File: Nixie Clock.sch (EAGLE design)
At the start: 153 parts, among them IC1_SECONDS_UNITS 4017N, IC2_SECONDS_TENS 4017N, IC3_MINUTES_UNITS 4017N, IC4_MINUTES_TENS 4017N, IC5_HOURS_UNITS 4017N, IC6_HOURS_TENS 4017N, IC7_AND 4081N, T0 MPSA42, T1 MPSA42, T10 MPSA42, T11 MPSA42, T12 MPSA42, T13 MPSA42, T14 MPSA42, T15 MPSA42, T16 MPSA42, T17 MPSA42, T18 MPSA42, T19 MPSA42, T2 MPSA42, T20 MPSA42, T21 MPSA42, T22 MPSA42, T23 MPSA42, T24 MPSA42, T25 MPSA42, T26 MPSA42, T27 MPSA42, T28 MPSA42, T29 MPSA42, T3 MPSA42, T30 MPSA42, T31 MPSA42, T32 MPSA42, T33 MPSA42, T34 MPSA42, T35 MPSA42, T36 MPSA42, T37 MPSA42, T38 MPSA42, T39 MPSA42, T4 MPSA42, T40 MPSA42, T41 MPSA42, T42 MPSA42, T43 MPSA42, T44 MPSA42, T5 MPSA42, T6 MPSA42, T7 MPSA42, T8 MPSA42, T9 MPSA42

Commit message: Use an alternative package for tubes, with bigger pads
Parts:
- HOURS_TENS, HOURS_UNITS, MINUTES_TENS, MINUTES_UNITS, SECONDS_TENS, SECONDS_UNITS: value IN-14 -> IN-14BIG_PADS; device PGT:IN-14 -> PGT:IN-14BIG_PADS
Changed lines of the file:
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@@
 <grid distance="0.1" unitdist="inch" unit="inch" style="lines" multiple="1" display="no" altdistance="0.01" altunitdist="inch" altunit="inch"/>
 <layers>
-<layer number="1" name="Top" color="4" fill="1" visible="no" active="no"/>
-<layer number="2" name="Route2" color="1" fill="3" visible="no" active="no"/>
-<layer number="3" name="Route3" color="4" fill="3" visible="no" active="no"/>
-<layer number="4" name="Route4" color="1" fill="4" visible="no" active="no"/>
-<layer number="5" name="Route5" color="4" fill="4" visible="no" active="no"/>
-<layer number="6" name="Route6" color="1" fill="8" visible="no" active="no"/>
-<layer number="7" name="Route7" color="4" fill="8" visible="no" active="no"/>
-<layer number="8" name="Route8" color="1" fill="2" visible="no" active="no"/>
-<layer number="9" name="Route9" color="4" fill="2" visible="no" active="no"/>
-<layer number="10" name="Route10" color="1" fill="7" visible="no" active="no"/>
-<layer number="11" name="Route11" color="4" fill="7" visible="no" active="no"/>
-<layer number="12" name="Route12" color="1" fill="5" visible="no" active="no"/>
-<layer number="13" name="Route13" color="4" fill="5" visible="no" active="no"/>
-<layer number="14" name="Route14" color="1" fill="6" visible="no" active="no"/>
-<layer number="15" name="Route15" color="4" fill="6" visible="no" active="no"/>
-<layer number="16" name="Bottom" color="1" fill="1" visible="no" active="no"/>
-<layer number="17" name="Pads" color="2" fill="1" visible="no" active="no"/>
-<layer number="18" name="Vias" color="2" fill="1" visible="no" active="no"/>
-<layer number="19" name="Unrouted" color="6" fill="1" visible="no" active="no"/>
-<layer number="20" name="Dimension" color="15" fill="1" visible="no" active="no"/>
-<layer number="21" name="tPlace" color="7" fill="1" visible="no" active="no"/>
-<layer number="22" name="bPlace" color="7" fill="1" visible="no" active="no"/>
-<layer number="23" name="tOrigins" color="15" fill="1" visible="no" active="no"/>
-<layer number="24" name="bOrigins" color="15" fill="1" visible="no" active="no"/>
-<layer number="25" name="tNames" color="7" fill="1" visible="no" active="no"/>
-<layer number="26" name="bNames" color="7" fill="1" visible="no" active="no"/>
-<layer number="27" name="tValues" color="7" fill="1" visible="no" active="no"/>
-<layer number="28" name="bValues" color="7" fill="1" visible="no" active="no"/>
+<layer number="1" name="Top" color="4" fill="1" visible="yes" active="no"/>
+<layer number="2" name="Route2" color="1" fill="3" visible="yes" active="no"/>
+<layer number="3" name="Route3" color="4" fill="3" visible="yes" active="no"/>
+<layer number="4" name="Route4" color="1" fill="4" visible="yes" active="no"/>
+<layer number="5" name="Route5" color="4" fill="4" visible="yes" active="no"/>
+<layer number="6" name="Route6" color="1" fill="8" visible="yes" active="no"/>
+<layer number="7" name="Route7" color="4" fill="8" visible="yes" active="no"/>
+<layer number="8" name="Route8" color="1" fill="2" visible="yes" active="no"/>
+<layer number="9" name="Route9" color="4" fill="2" visible="yes" active="no"/>
+<layer number="10" name="Route10" color="1" fill="7" visible="yes" active="no"/>
+<layer number="11" name="Route11" color="4" fill="7" visible="yes" active="no"/>
+<layer number="12" name="Route12" color="1" fill="5" visible="yes" active="no"/>
+<layer number="13" name="Route13" color="4" fill="5" visible="yes" active="no"/>
+<layer number="14" name="Route14" color="1" fill="6" visible="yes" active="no"/>
+<layer number="15" name="Route15" color="4" fill="6" visible="yes" active="no"/>
+<layer number="16" name="Bottom" color="1" fill="1" visible="yes" active="no"/>
+<layer number="17" name="Pads" color="2" fill="1" visible="yes" active="no"/>
+<layer number="18" name="Vias" color="2" fill="1" visible="yes" active="no"/>
+<layer number="19" name="Unrouted" color="6" fill="1" visible="yes" active="no"/>
+<layer number="20" name="Dimension" color="15" fill="1" visible="yes" active="no"/>
+<layer number="21" name="tPlace" color="7" fill="1" visible="yes" active="no"/>
+<layer number="22" name="bPlace" color="7" fill="1" visible="yes" active="no"/>
+<layer number="23" name="tOrigins" color="15" fill="1" visible="yes" active="no"/>
+<layer number="24" name="bOrigins" color="15" fill="1" visible="yes" active="no"/>
+<layer number="25" name="tNames" color="7" fill="1" visible="yes" active="no"/>
+<layer number="26" name="bNames" color="7" fill="1" visible="yes" active="no"/>
+<layer number="27" name="tValues" color="7" fill="1" visible="yes" active="no"/>
+<layer number="28" name="bValues" color="7" fill="1" visible="yes" active="no"/>
 <layer number="29" name="tStop" color="7" fill="3" visible="no" active="no"/>
 <layer number="30" name="bStop" color="7" fill="6" visible="no" active="no"/>
@@
 <layer number="35" name="tGlue" color="7" fill="4" visible="no" active="no"/>
 <layer number="36" name="bGlue" color="7" fill="5" visible="no" active="no"/>
-<layer number="37" name="tTest" color="7" fill="1" visible="no" active="no"/>
-<layer number="38" name="bTest" color="7" fill="1" visible="no" active="no"/>
+<layer number="37" name="tTest" color="7" fill="1" visible="yes" active="no"/>
+<layer number="38" name="bTest" color="7" fill="1" visible="yes" active="no"/>
 <layer number="39" name="tKeepout" color="4" fill="11" visible="no" active="no"/>
 <layer number="40" name="bKeepout" color="1" fill="11" visible="no" active="no"/>
@@
 <layer number="44" name="Drills" color="7" fill="1" visible="no" active="no"/>
 <layer number="45" name="Holes" color="7" fill="1" visible="no" active="no"/>
-<layer number="46" name="Milling" color="3" fill="1" visible="no" active="no"/>
-<layer number="47" name="Measures" color="7" fill="1" visible="no" active="no"/>
-<layer number="48" name="Document" color="7" fill="1" visible="no" active="no"/>
-<layer number="49" name="Reference" color="7" fill="1" visible="no" active="no"/>
-<layer number="50" name="dxf" color="7" fill="1" visible="no" active="no"/>
-<layer number="51" name="tDocu" color="7" fill="1" visible="no" active="no"/>
-<layer number="52" name="bDocu" color="7" fill="1" visible="no" active="no"/>
-<layer number="53" name="tGND_GNDA" color="7" fill="9" visible="no" active="no"/>
-<layer number="54" name="bGND_GNDA" color="1" fill="9" visible="no" active="no"/>
-<layer number="56" name="wert" color="7" fill="1" visible="no" active="no"/>
-<layer number="57" name="tCAD" color="7" fill="1" visible="no" active="no"/>
+<layer number="46" name="Milling" color="3" fill="1" visible="yes" active="no"/>
+<layer number="47" name="Measures" color="7" fill="1" visible="yes" active="no"/>
+<layer number="48" name="Document" color="7" fill="1" visible="yes" active="no"/>
+<layer number="49" name="Reference" color="7" fill="1" visible="yes" active="no"/>
+<layer number="50" name="dxf" color="7" fill="1" visible="yes" active="no"/>
+<layer number="51" name="tDocu" color="7" fill="1" visible="yes" active="no"/>
+<layer number="52" name="bDocu" color="7" fill="1" visible="yes" active="no"/>
+<layer number="53" name="tGND_GNDA" color="7" fill="9" visible="yes" active="no"/>
+<layer number="54" name="bGND_GNDA" color="1" fill="9" visible="yes" active="no"/>
+<layer number="56" name="wert" color="7" fill="1" visible="yes" active="no"/>
+<layer number="57" name="tCAD" color="7" fill="1" visible="yes" active="no"/>
 <layer number="90" name="Modules" color="5" fill="1" visible="yes" active="yes"/>
 <layer number="91" name="Nets" color="2" fill="1" visible="yes" active="yes"/>
@@
 <parts>
 <part name="FRAME1" library="frames" deviceset="LETTER_L" device="" value="TUBES_FOR_SECONDS"/>
-<part name="SECONDS_UNITS" library="PGT" deviceset="IN-14" device=""/>
-<part name="SECONDS_TENS" library="PGT" deviceset="IN-14" device=""/>
+<part name="SECONDS_UNITS" library="PGT" deviceset="IN-14" device="BIG_PADS" value="IN-14BIG_PADS"/>
+<part name="SECONDS_TENS" library="PGT" deviceset="IN-14" device="BIG_PADS" value="IN-14BIG_PADS"/>
 <part name="T1" library="PGT" deviceset="MPSA42" device=""/>
 <part name="T2" library="PGT" deviceset="MPSA42" device=""/>
@@
 <part name="SUPPLY4" library="supply2" deviceset="GND" device=""/>
 <part name="FRAME2" library="frames" deviceset="LETTER_L" device="" value="TUBES_FOR_MINUTES"/>
-<part name="MINUTES_UNITS" library="PGT" deviceset="IN-14" device=""/>
-<part name="MINUTES_TENS" library="PGT" deviceset="IN-14" device=""/>
+<part name="MINUTES_UNITS" library="PGT" deviceset="IN-14" device="BIG_PADS" value="IN-14BIG_PADS"/>
+<part name="MINUTES_TENS" library="PGT" deviceset="IN-14" device="BIG_PADS" value="IN-14BIG_PADS"/>
 <part name="T16" library="PGT" deviceset="MPSA42" device=""/>
 <part name="T17" library="PGT" deviceset="MPSA42" device=""/>
@@
 <part name="SUPPLY8" library="supply2" deviceset="GND" device=""/>
 <part name="FRAME3" library="frames" deviceset="LETTER_L" device="" value="TUBES_FOR_HOURS"/>
-<part name="HOURS_UNITS" library="PGT" deviceset="IN-14" device=""/>
-<part name="HOURS_TENS" library="PGT" deviceset="IN-14" device=""/>
+<part name="HOURS_UNITS" library="PGT" deviceset="IN-14" device="BIG_PADS" value="IN-14BIG_PADS"/>
+<part name="HOURS_TENS" library="PGT" deviceset="IN-14" device="BIG_PADS" value="IN-14BIG_PADS"/>
 <part name="T32" library="PGT" deviceset="MPSA42" device=""/>
 <part name="T33" library="PGT" deviceset="MPSA42" device=""/>

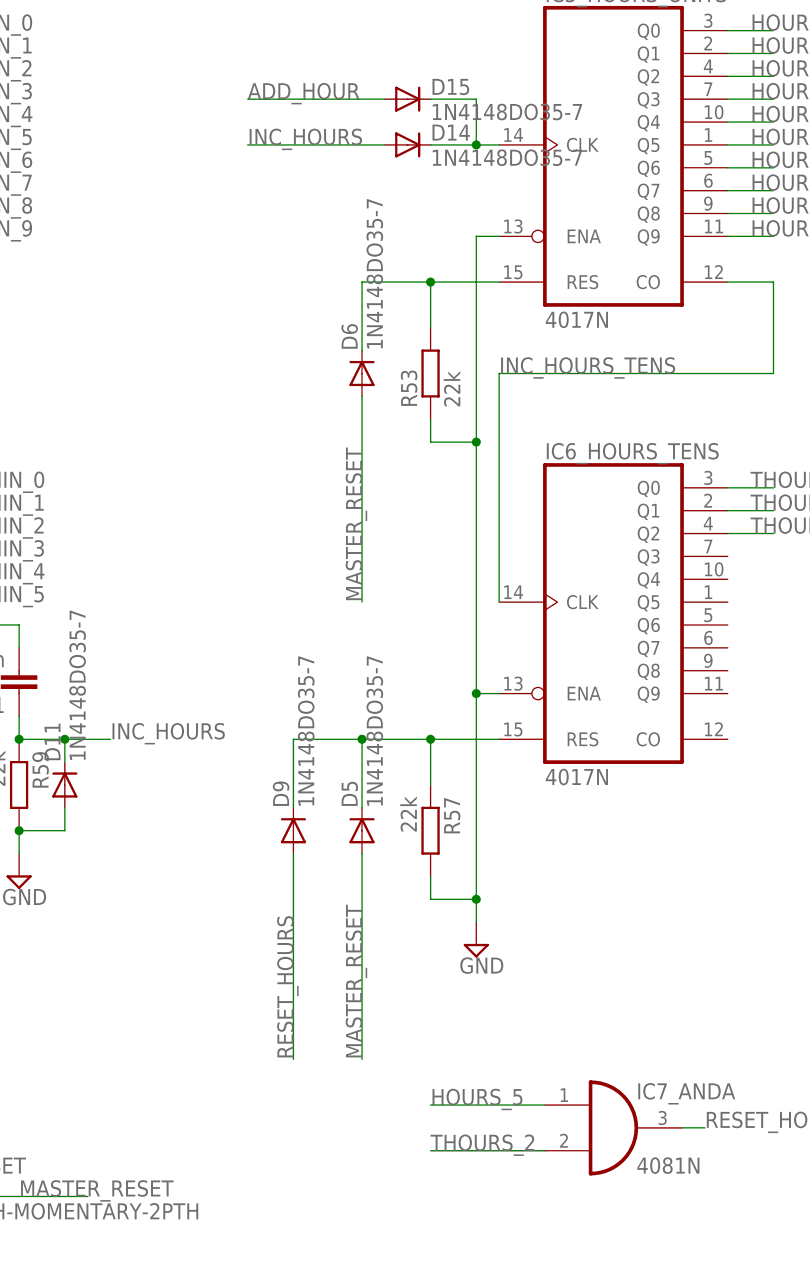
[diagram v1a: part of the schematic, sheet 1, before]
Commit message: Fix RESET_HOURS signal in schematics and layout
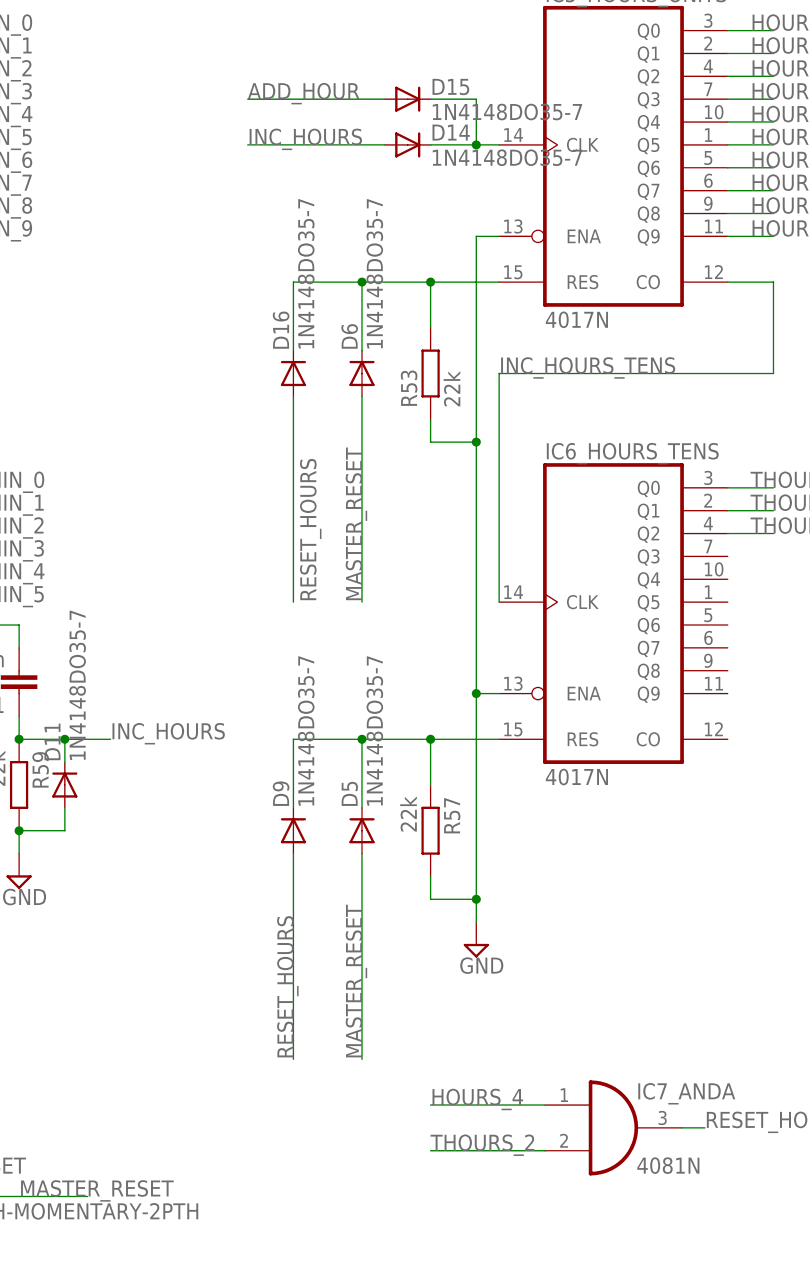
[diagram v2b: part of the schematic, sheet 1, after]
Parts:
- added D16: 1N4148DO35-7, diode:1N4148DO35-7
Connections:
- removed net N$106: D6.C, IC5_HOURS_UNITSA.RES, R53.2
- new net N$109: D16.C, D6.C, IC5_HOURS_UNITSA.RES, R53.2
- net HOURS_4: now also IC7_ANDA.I0
- net HOURS_5: no longer IC7_ANDA.I0
- net RESET_HOURS: now also D16.A
